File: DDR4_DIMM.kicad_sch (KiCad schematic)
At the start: 0 parts

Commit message: Making DDR4 DRAM footprint
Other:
- added sheet Untitled Sheet (untitled.kicad_sch)
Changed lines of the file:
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@@
 	(generator_version "9.0")
 	(paper "A4")
+	(sheet
+		(at 31.75 33.02)
+		(size 53.34 30.48)
+		(exclude_from_sim no)
+		(in_bom yes)
+		(on_board yes)
+		(dnp no)
+		(fields_autoplaced yes)
+		(stroke
+			(width 0.1524)
+			(type solid)
+		)
+		(fill
+			(color 0 0 0 0.0000)
+		)
+		(property "Sheetname" "Untitled Sheet"
+			(at 31.75 32.3084 0)
+			(effects
+				(font
+					(size 1.27 1.27)
+				)
+				(justify left bottom)
+			)
+		)
+		(property "Sheetfile" "untitled.kicad_sch"
+			(at 31.75 64.0846 0)
+			(effects
+				(font
+					(size 1.27 1.27)
+				)
+				(justify left top)
+			)
+		)
+		(instances
+			(project "DDR4_DIMM"
+				(path "/2162f80d-5bbc-406a-8824-9611d78b7103"
+					(page "2")
+				)
+			)
+		)
+	)
 	(sheet_instances
 		(path "/"

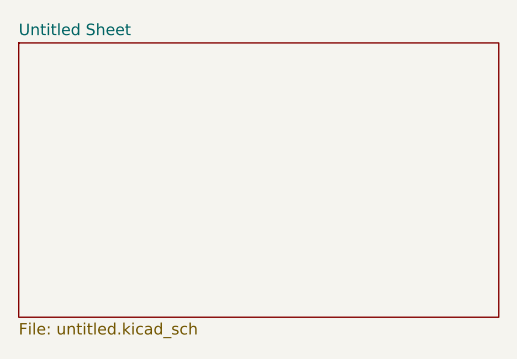
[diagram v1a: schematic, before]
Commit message: Modifying DIMM Edge connector Footprint
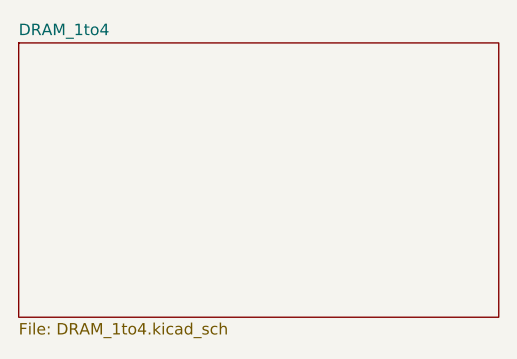
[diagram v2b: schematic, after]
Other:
- sheet Untitled Sheet renamed DRAM_1to4
- sheet DRAM_1to4: file untitled.kicad_sch -> DRAM_1to4.kicad_sch
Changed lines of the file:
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@@
 			(color 0 0 0 0.0000)
 		)
-		(property "Sheetname" "Untitled Sheet"
+		(property "Sheetname" "DRAM_1to4"
 			(at 31.75 32.3084 0)
 			(effects
@@
 			)
 		)
-		(property "Sheetfile" "untitled.kicad_sch"
+		(property "Sheetfile" "DRAM_1to4.kicad_sch"
 			(at 31.75 64.0846 0)
 			(effects

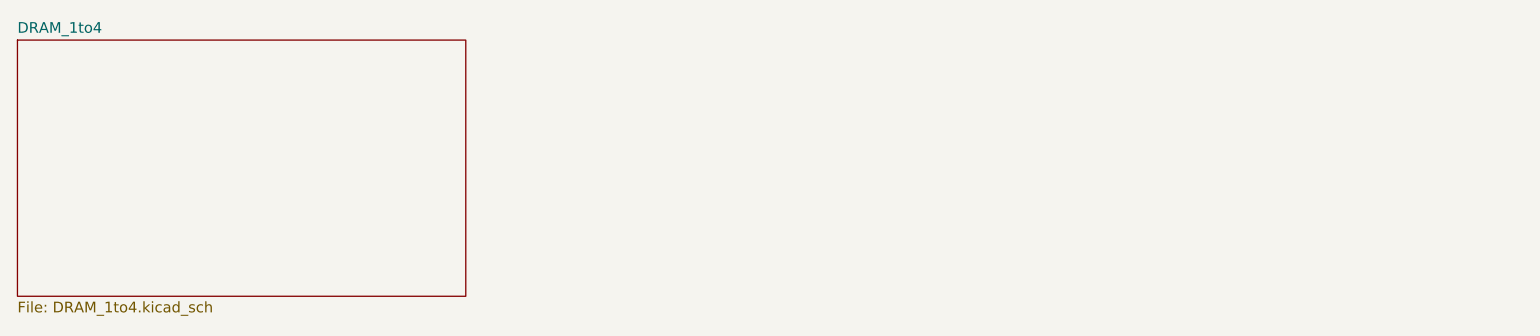
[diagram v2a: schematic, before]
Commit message: Adding Edge connector schematic
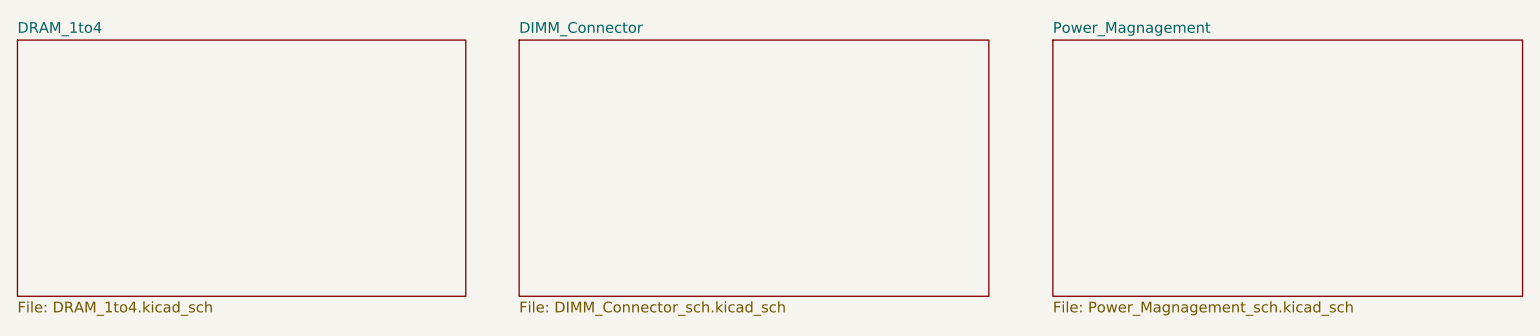
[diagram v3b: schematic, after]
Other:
- added sheet DIMM_Connector (DIMM_Connector_sch.kicad_sch)
- added sheet Power_Magnagement (Power_Magnagement_sch.kicad_sch)
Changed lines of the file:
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@@
 (kicad_sch
-	(version 20250114)
+	(version 20260306)
 	(generator "eeschema")
-	(generator_version "9.0")
+	(generator_version "10.0")
 	(paper "A4")
+	(sheet
+		(at 91.44 33.02)
+		(size 55.88 30.48)
+		(exclude_from_sim no)
+		(in_bom yes)
+		(on_board yes)
+		(dnp no)
+		(fields_autoplaced yes)
+		(stroke
+			(width 0.1524)
+			(type solid)
+		)
+		(fill
+			(color 0 0 0 0)
+		)
+		(property "Sheetname" "DIMM_Connector"
+			(at 91.44 32.3084 0)
+			(show_name no)
+			(do_not_autoplace no)
+			(effects
+				(font
+					(size 1.27 1.27)
+				)
+				(justify left bottom)
+			)
+		)
+		(property "Sheetfile" "DIMM_Connector_sch.kicad_sch"
+			(at 91.44 64.0846 0)
+			(show_name no)
+			(do_not_autoplace no)
+			(effects
+				(font
+					(size 1.27 1.27)
+				)
+				(justify left top)
+			)
+		)
+		(instances
+			(project "DDR4_DIMM"
+				(path "/2162f80d-5bbc-406a-8824-9611d78b7103"
+					(page "3")
+				)
+			)
+		)
+	)
 	(sheet
 		(at 31.75 33.02)
@@
 		)
 		(fill
-			(color 0 0 0 0.0000)
+			(color 0 0 0 0)
 		)
 		(property "Sheetname" "DRAM_1to4"
 			(at 31.75 32.3084 0)
+			(show_name no)
+			(do_not_autoplace no)
 			(effects
 				(font
@@
 		(property "Sheetfile" "DRAM_1to4.kicad_sch"
 			(at 31.75 64.0846 0)
+			(show_name no)
+			(do_not_autoplace no)
 			(effects
 				(font
@@
 				)
 			)
+		)
+	)
+	(sheet
+		(at 154.94 33.02)
+		(size 55.88 30.48)
+		(exclude_from_sim no)
+		(in_bom yes)
+		(on_board yes)
+		(dnp no)
+		(fields_autoplaced yes)
+		(stroke
+			(width 0.1524)
+			(type solid)
+		)
+		(fill
+			(color 0 0 0 0)
+		)
+		(property "Sheetname" "Power_Magnagement"
+			(at 154.94 32.3084 0)
+			(show_name no)
+			(do_not_autoplace no)
+			(effects
+				(font
+					(size 1.27 1.27)
+				)
+				(justify left bottom)
+			)
+		)
+		(property "Sheetfile" "Power_Magnagement_sch.kicad_sch"
+			(at 154.94 64.0846 0)
+			(show_name no)
+			(do_not_autoplace no)
+			(effects
+				(font
+					(size 1.27 1.27)
+				)
+				(justify left top)
+			)
+		)
+		(instances
+			(project "DDR4_DIMM"
+				(path "/2162f80d-5bbc-406a-8824-9611d78b7103"
+					(page "4")
+				)
+			)
